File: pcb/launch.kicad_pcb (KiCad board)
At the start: 4 copper layers, 299 x 127 mm, 372 parts, among them J0 12401598E4#2A, J1 DNP, J2 1003-002-01100, J3 1003-002-01100, J4 12401598E4#2A, J5 12401598E4#2A, U0 USBLC6-2SC6, U1 ATmega32U4-MU, U10 AP22811AW5-7, U11 PTN5110DHQ, U12 PTN5110THQ, U13 PTN5110THQ, U14 SN74LVC1G08DCKR, U15 CBTL02043ABQ,115, U16 AP22811AW5-7‎, U17 AP3441LSHE-7B, U18 LP5907MFX-3.3, U19 SN74LVC1G08DCKR, U2 USB7206, U20 AP22811AW5-7, U21 USBLC6-2SC6, U22 AP22811AW5-7, U23 AP22811AW5-7, U3 CBTL02043ABQ,115, U4 AP3441LSHE-7B, U5 USBLC6-2SC6, U6 CBTL02043ABQ,115, U7 USBLC6-2SC6, U8 USBLC6-2SC6, U9 AP22811AW5-7, X1 ECS-3225MV-250-BN-TR, Y0 ECS-160-18-23G-JGN-TR

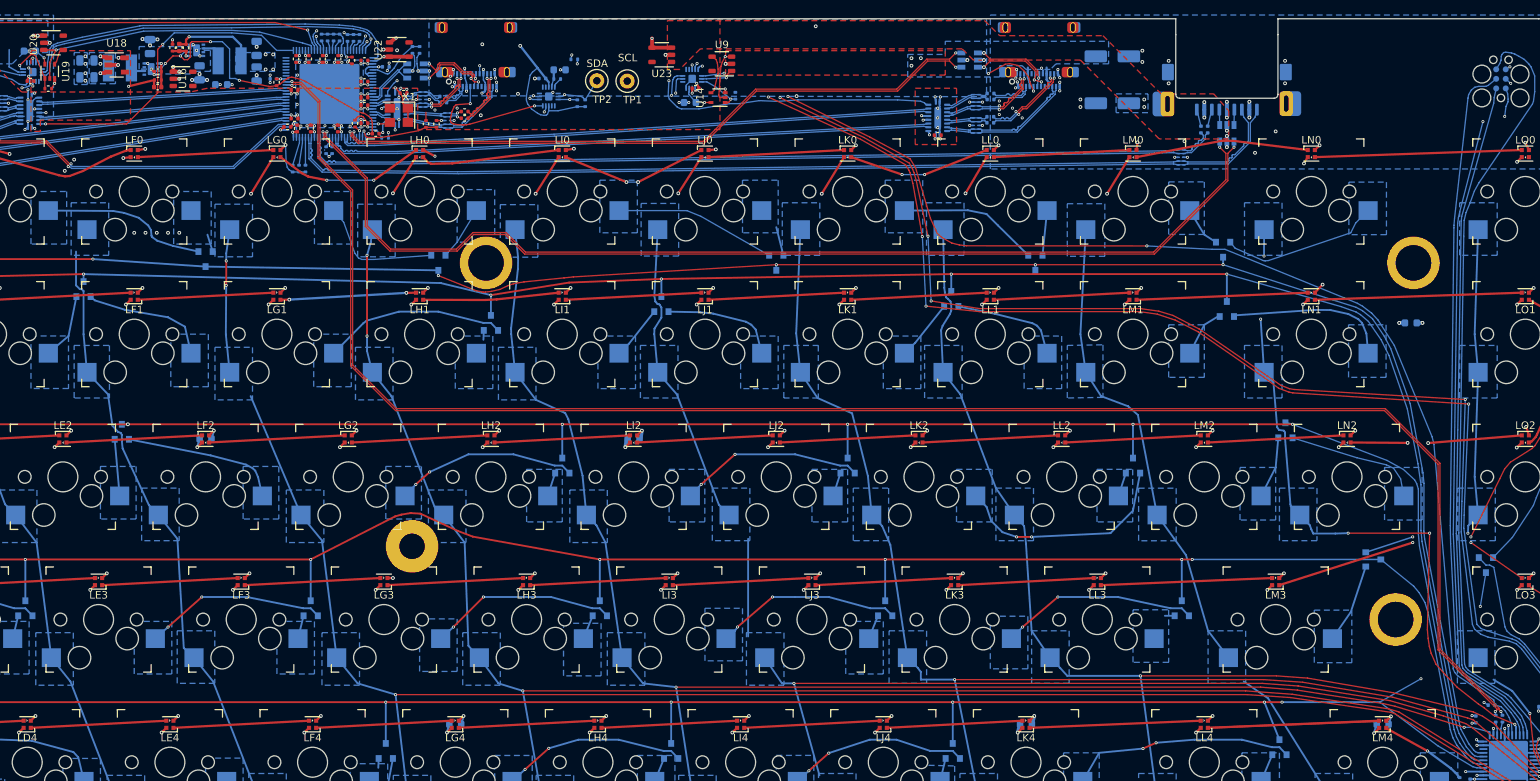
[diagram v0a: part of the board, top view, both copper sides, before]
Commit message: Use AP61302 for regulating 1V1 and 3V6 power planes
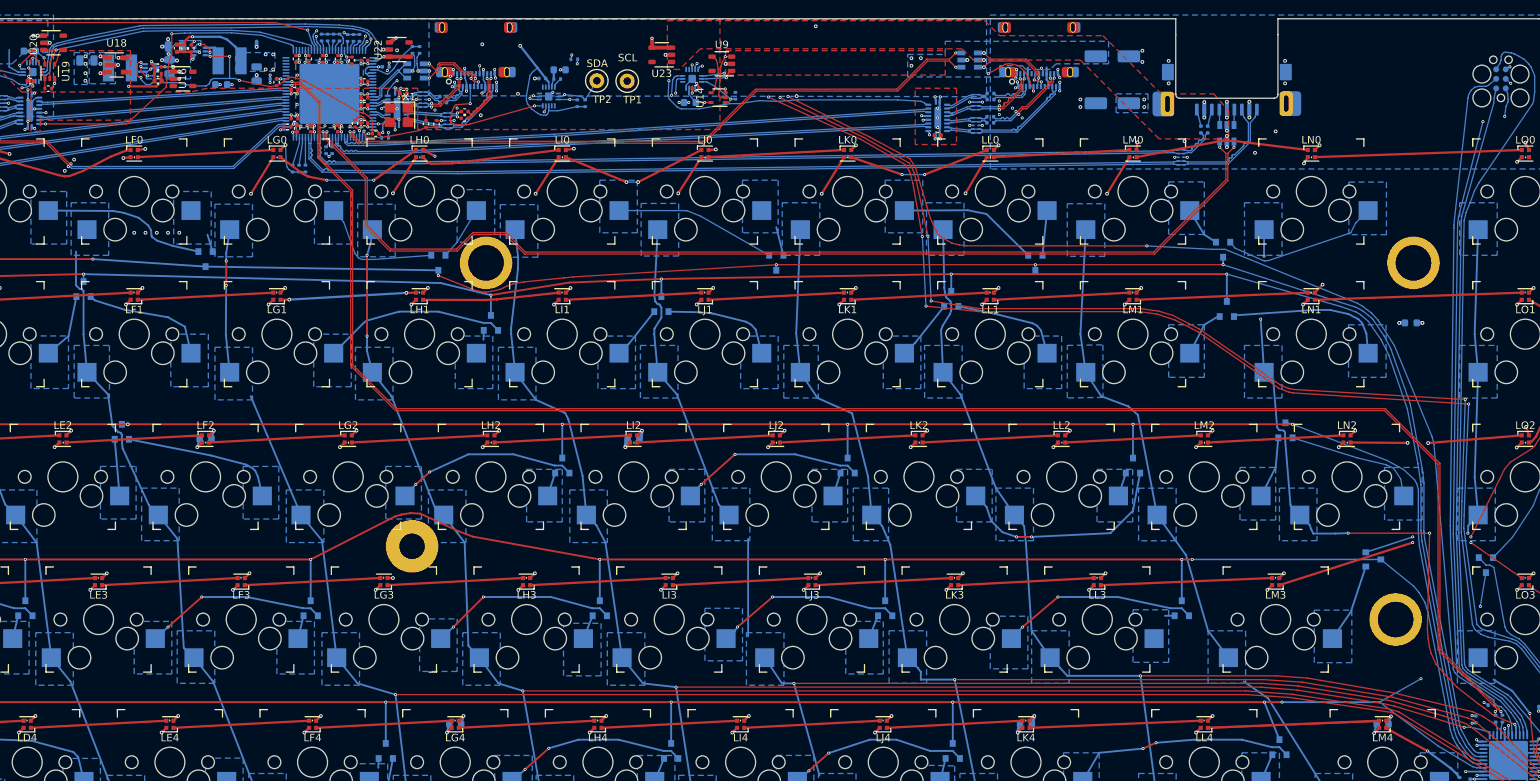
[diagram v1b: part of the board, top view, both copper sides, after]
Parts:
- removed C35, C50: 22 uF, Capacitor_SMD:C_0805_2012Metric
- U17, U4: value AP3441LSHE-7B -> AP61302; footprint launch:W-DFN2020-8_Type_C -> launch:SOT-563
- moved C32 4.74 mm to (110.5, -9.30), turned to 180 degrees
- moved C48 3.75 mm to (109.7, -6.60)
- moved R15 2.50 mm to (112.6, -9.05)
- moved R25 0.85 mm to (108.2, -5.70), turned to 180 degrees
- moved C69 0.80 mm to (108.2, -4.70), turned to 180 degrees
- moved R26 0.65 mm to (108.2, -6.60), turned to 0 degrees
- moved U17 0.43 mm to (113.7, -8.65)
- moved C68 0.32 mm to (110.7, -9.08)
- moved R14 0.22 mm to (111.7, -9.05)
- moved U4 0.15 mm to (107.2, -6.45)
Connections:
- J0 pad A8: Net-(J0-PadA8) -> (no net)
- J0 pad B8: Net-(J0-PadB8) -> (no net)
- J4 pad A8: Net-(J4-PadA8) -> (no net)
- J4 pad B8: Net-(J4-PadB8) -> (no net)
- J5 pad A8: Net-(J5-PadA8) -> (no net)
- J5 pad B8: Net-(J5-PadB8) -> (no net)
- LO0 pad 3: Net-(LO0-Pad3) -> (no net)
- U1 pad 2: Net-(U1-Pad2) -> (no net)
- U1 pad 42: Net-(U1-Pad42) -> (no net)
- U11 pad 1: Net-(U11-Pad1) -> (no net)
- U11 pad 10: Net-(U11-Pad10) -> (no net)
- U11 pad 16: Net-(U11-Pad16) -> (no net)
- U11 pad 2: Net-(U11-Pad2) -> (no net)
- U11 pad 6: Net-(U11-Pad6) -> (no net)
- U11 pad 9: Net-(U11-Pad9) -> (no net)
- U12 pad 1: Net-(U12-Pad1) -> (no net)
- U12 pad 10: Net-(U12-Pad10) -> (no net)
- U12 pad 2: Net-(U12-Pad2) -> (no net)
- U12 pad 6: Net-(U12-Pad6) -> (no net)
- U12 pad 9: Net-(U12-Pad9) -> (no net)
- U13 pad 1: Net-(U13-Pad1) -> (no net)
- U13 pad 10: Net-(U13-Pad10) -> (no net)
- U13 pad 2: Net-(U13-Pad2) -> (no net)
- U13 pad 5: Net-(U13-Pad5) -> (no net)
- U13 pad 6: Net-(U13-Pad6) -> (no net)
- U13 pad 9: Net-(U13-Pad9) -> (no net)
- U16 pad 3: Net-(U16-Pad3) -> (no net)
- U17 pad 2: /USB/~RESET -> GND
- U17 pad 4: GND -> /power/SW1V1
- U17 pad 5: (no net) -> VCC
- U17 pad 6: /power/SW1V1 -> /USB/~RESET
- U18 pad 4: Net-(U18-Pad4) -> (no net)
- U2 pad 4: Net-(U2-Pad4) -> (no net)
- U2 pad 44: Net-(U2-Pad44) -> (no net)
- U2 pad 45: Net-(U2-Pad45) -> (no net)
- U2 pad 46: Net-(U2-Pad46) -> (no net)
- U2 pad 47: Net-(U2-Pad47) -> (no net)
- U2 pad 48: Net-(U2-Pad48) -> (no net)
- U2 pad 49: Net-(U2-Pad49) -> (no net)
- U2 pad 50: Net-(U2-Pad50) -> (no net)
- U2 pad 52: Net-(U2-Pad52) -> (no net)
- U2 pad 54: Net-(U2-Pad54) -> (no net)
- U2 pad 56: /USB/PRT_CTL5 -> (no net)
- U2 pad 66: Net-(U2-Pad66) -> (no net)
- U2 pad 72: Net-(U2-Pad72) -> (no net)
- U2 pad 83: Net-(U2-Pad83) -> (no net)
- U2 pad 84: Net-(U2-Pad84) -> (no net)
- U2 pad 86: Net-(U2-Pad86) -> (no net)
- U2 pad 87: Net-(U2-Pad87) -> (no net)
- U2 pad 96: Net-(U2-Pad96) -> (no net)
- U2 pad 97: /USB/XTALO -> (no net)
- U4 pad 2: /USB/~RESET -> GND
- U4 pad 4: GND -> /power/SW3V6
- U4 pad 5: (no net) -> VCC
- U4 pad 6: /power/SW3V6 -> /USB/~RESET
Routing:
- net VCC: track 1.45 -> 9.07 mm, vias 2 -> 6
- net /USB/~RESET: track 42.4 -> 46.8 mm, vias 5 -> 6
- net GND: track 250.1 -> 246.2 mm, vias 277 -> 273
- net /power/SW1V1: track 1.55 -> 3.24 mm
- net +3V6: track 148.9 -> 150.1 mm
- net Net-(U1-Pad2): track 0.91 -> 0.00 mm, vias 1 -> 0
- net /power/FB1V1: track 2.95 -> 3.60 mm
- net +1V1: track 22.3 -> 21.8 mm
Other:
- board text added: "Launch Rev 1.3 Board must be RoHS compliant Fabricate to IPC-A-600 Class II Material: Shengyi S1000-2 Inner copper 1 or 1/2 oz Outer copper, min 33.4 um finished Black LPI solder mask over bare copper Vendor may remove solder mask from via holes, maximum of drill size + 3 mil Finish: OSP Silkscreen: white non conductive 100% electrical test required Remove all unused pads from inner layers All la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"
- board text added: "launch_1.3"
- board text removed: "Launch Rev 1.2 Board must be RoHS compliant Fabricate to IPC-A-600 Class II Material: Shengyi S1000-2 Inner copper 1 or 1/2 oz Outer copper, min 33.4 um finished Black LPI solder mask over bare copper Vendor may remove solder mask from via holes, maximum of drill size + 3 mil Finish: OSP Silkscreen: white non conductive 100% electrical test required Remove all unused pads from inner layers All la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"
- board text removed: "launch_1.2"

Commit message: minor layout adjustments, feedforward cap value Change feedforward cap to 330 pF so the transfer function of the feedback   network will be similar to that of the datasheet example. Our feedback   resistors are lower and the impedance of the cap needs to be proportionally   lower.
Correct typo in notes on power schematic page.

Change buck feedforward cap footprint from Kicad lib to launch lib for consistency.

Arrange schematic components so "330 pF" does not overlap adjacent components.

Move "U4" silkscreen to not overlap inductor pad.

Add a 2nd via to each buck converter ground, move feedback components to allow.

Reroute some signal traces to reduce number of vias, have more solid ground
  planes around the buck converters. This included CL_SEL, RESET, VCC (to enable).
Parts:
- C68, C69: value 22 pF -> 330 pF; footprint Capacitor_SMD:C_0402_1005Metric -> launch:C_0402_1005Metric
- moved R15 1.79 mm to (111.8, -7.45), turned to 180 degrees
- moved C69 1.42 mm to (106.8, -5.20), turned to 90 degrees
- moved R26 1.31 mm to (107.8, -7.85)
- moved R25 0.52 mm to (108.0, -5.20), turned to 90 degrees
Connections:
- J0 pad A8: (no net) -> Net-(J0-PadA8)
- J0 pad B8: (no net) -> Net-(J0-PadB8)
- J4 pad A8: (no net) -> Net-(J4-PadA8)
- J4 pad B8: (no net) -> Net-(J4-PadB8)
- J5 pad A8: (no net) -> Net-(J5-PadA8)
- J5 pad B8: (no net) -> Net-(J5-PadB8)
- LO0 pad 3: (no net) -> Net-(LO0-Pad3)
- U1 pad 2: (no net) -> Net-(U1-Pad2)
- U1 pad 42: (no net) -> Net-(U1-Pad42)
- U11 pad 1: (no net) -> Net-(U11-Pad1)
- U11 pad 10: (no net) -> Net-(U11-Pad10)
- U11 pad 16: (no net) -> Net-(U11-Pad16)
- U11 pad 2: (no net) -> Net-(U11-Pad2)
- U11 pad 6: (no net) -> Net-(U11-Pad6)
- U11 pad 9: (no net) -> Net-(U11-Pad9)
- U12 pad 1: (no net) -> Net-(U12-Pad1)
- U12 pad 10: (no net) -> Net-(U12-Pad10)
- U12 pad 2: (no net) -> Net-(U12-Pad2)
- U12 pad 6: (no net) -> Net-(U12-Pad6)
- U12 pad 9: (no net) -> Net-(U12-Pad9)
- U13 pad 1: (no net) -> Net-(U13-Pad1)
- U13 pad 10: (no net) -> Net-(U13-Pad10)
- U13 pad 2: (no net) -> Net-(U13-Pad2)
- U13 pad 5: (no net) -> Net-(U13-Pad5)
- U13 pad 6: (no net) -> Net-(U13-Pad6)
- U13 pad 9: (no net) -> Net-(U13-Pad9)
- U16 pad 3: (no net) -> Net-(U16-Pad3)
- U18 pad 4: (no net) -> Net-(U18-Pad4)
- U2 pad 4: (no net) -> Net-(U2-Pad4)
- U2 pad 44: (no net) -> Net-(U2-Pad44)
- U2 pad 45: (no net) -> Net-(U2-Pad45)
- U2 pad 46: (no net) -> Net-(U2-Pad46)
- U2 pad 47: (no net) -> Net-(U2-Pad47)
- U2 pad 48: (no net) -> Net-(U2-Pad48)
- U2 pad 49: (no net) -> Net-(U2-Pad49)
- U2 pad 50: (no net) -> Net-(U2-Pad50)
- U2 pad 52: (no net) -> Net-(U2-Pad52)
- U2 pad 54: (no net) -> Net-(U2-Pad54)
- U2 pad 56: (no net) -> /USB/PRT_CTL5
- U2 pad 66: (no net) -> Net-(U2-Pad66)
- U2 pad 72: (no net) -> Net-(U2-Pad72)
- U2 pad 83: (no net) -> Net-(U2-Pad83)
- U2 pad 84: (no net) -> Net-(U2-Pad84)
- U2 pad 86: (no net) -> Net-(U2-Pad86)
- U2 pad 87: (no net) -> Net-(U2-Pad87)
- U2 pad 96: (no net) -> Net-(U2-Pad96)
- U2 pad 97: (no net) -> /USB/XTALO
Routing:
- net VCC: track 9.07 -> 3.29 mm, vias 6 -> 2
- net +3V6: track 150.1 -> 146.9 mm
- net /USB/~RESET: track 46.8 -> 45.0 mm, vias 6 -> 3
- net /power/FB3V6: track 3.60 -> 4.26 mm
- net GND: track 246.2 -> 246.1 mm, vias 273 -> 272
- added copper zone on B.Cu, net /power/SW1V1
- added copper zone on B.Cu, net /power/SW3V6

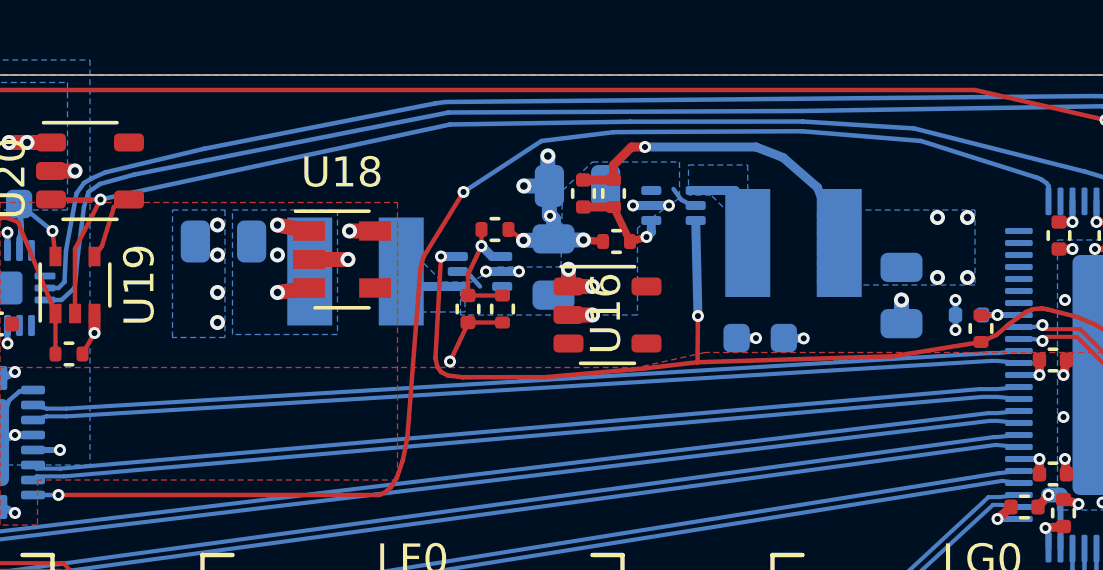
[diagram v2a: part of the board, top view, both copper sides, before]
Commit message: use AP3441LSHE-7B DC-DC switching to available part from long lead time part adds 2 22 uF 0805 capacitors as well
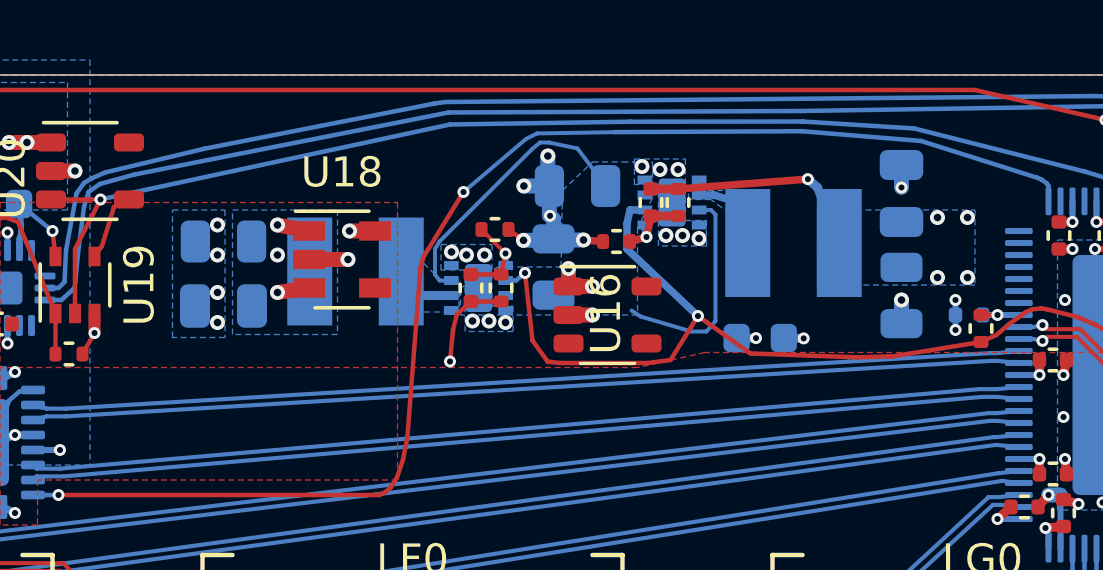
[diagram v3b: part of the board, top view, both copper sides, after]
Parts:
- added C35: 22 uF, Capacitor_SMD:C_0805_2012Metric, B.Cu at (98.7, -5.30)
- added C50: 22 uF, Capacitor_SMD:C_0805_2012Metric, B.Cu at (121.3, -9.05)
- U17, U4: value AP61302 -> AP3441LSHE-7B; footprint launch:SOT-563 -> launch:W-DFN2020-8_Type_C
- U2: value USB7206 -> USB7216C
- moved C68 2.27 mm to (113.0, -8.75)
- moved R14 2.17 mm to (113.8, -8.75)
- moved C69 0.71 mm to (107.0, -5.90)
- moved R25 0.70 mm to (108.0, -5.90)
- moved U4 0.55 mm to (107.2, -5.90)
- moved U17 0.11 mm to (113.7, -8.75)
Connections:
- U17 pad 2: GND -> /USB/~RESET
- U17 pad 4: /power/SW1V1 -> GND
- U17 pad 5: VCC -> (no net)
- U17 pad 6: /USB/~RESET -> /power/SW1V1
- U4 pad 2: GND -> /USB/~RESET
- U4 pad 4: /power/SW3V6 -> GND
- U4 pad 5: VCC -> (no net)
- U4 pad 6: /USB/~RESET -> /power/SW3V6
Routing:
- net VCC: track 3.29 -> 18.0 mm
- net +1V1: track 21.8 -> 18.5 mm
- net /USB/~RESET: track 45.0 -> 42.3 mm
- net GND: track 246.1 -> 244.6 mm, vias 272 -> 281
- net /power/FB3V6: track 4.26 -> 3.25 mm
- net /power/FB1V1: track 3.46 -> 2.69 mm
- net +3V6: track 146.9 -> 147.6 mm
- net /power/SW1V1: track 3.24 -> 2.72 mm
